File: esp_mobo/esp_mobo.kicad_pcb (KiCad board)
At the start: 2 copper layers, 75.5 x 107 mm, 54 parts, among them J1 Conn_01x04_Pin, J10 Conn_01x03_Pin, J11 Conn_01x03_Pin, J12 Conn_01x03_Pin, J13 Conn_01x03_Pin, J14 Conn_01x03_Pin, J15 Conn_01x03_Pin, J16 Conn_01x02_Pin, J2 Screw_Terminal_01x02, J3 Conn_01x03_Pin, J4 Conn_01x03_Pin, J5 Conn_01x03_Pin, J6 Conn_01x03_Pin, J7 Conn_01x03_Pin, J8 Conn_01x03_Pin, J9 Conn_01x03_Pin, U1 ESP32-DevKitC, U2 74AHCT125, U3 PC847, U4 PC847, U5 BME280

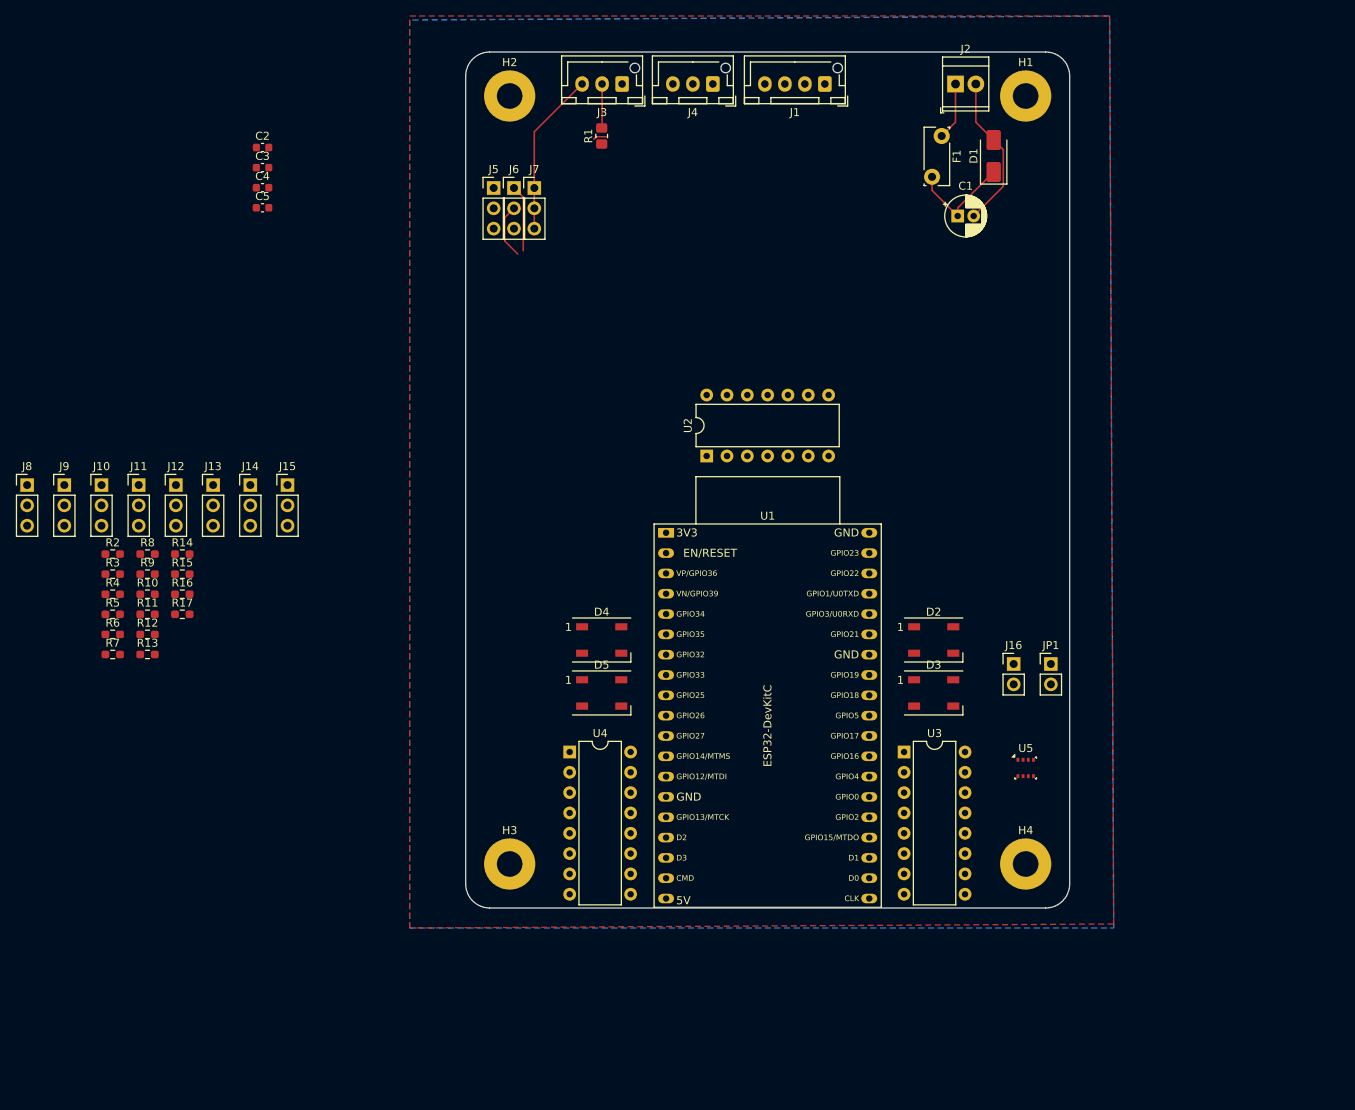
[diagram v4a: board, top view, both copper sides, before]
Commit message: Update ESC Mobo with board
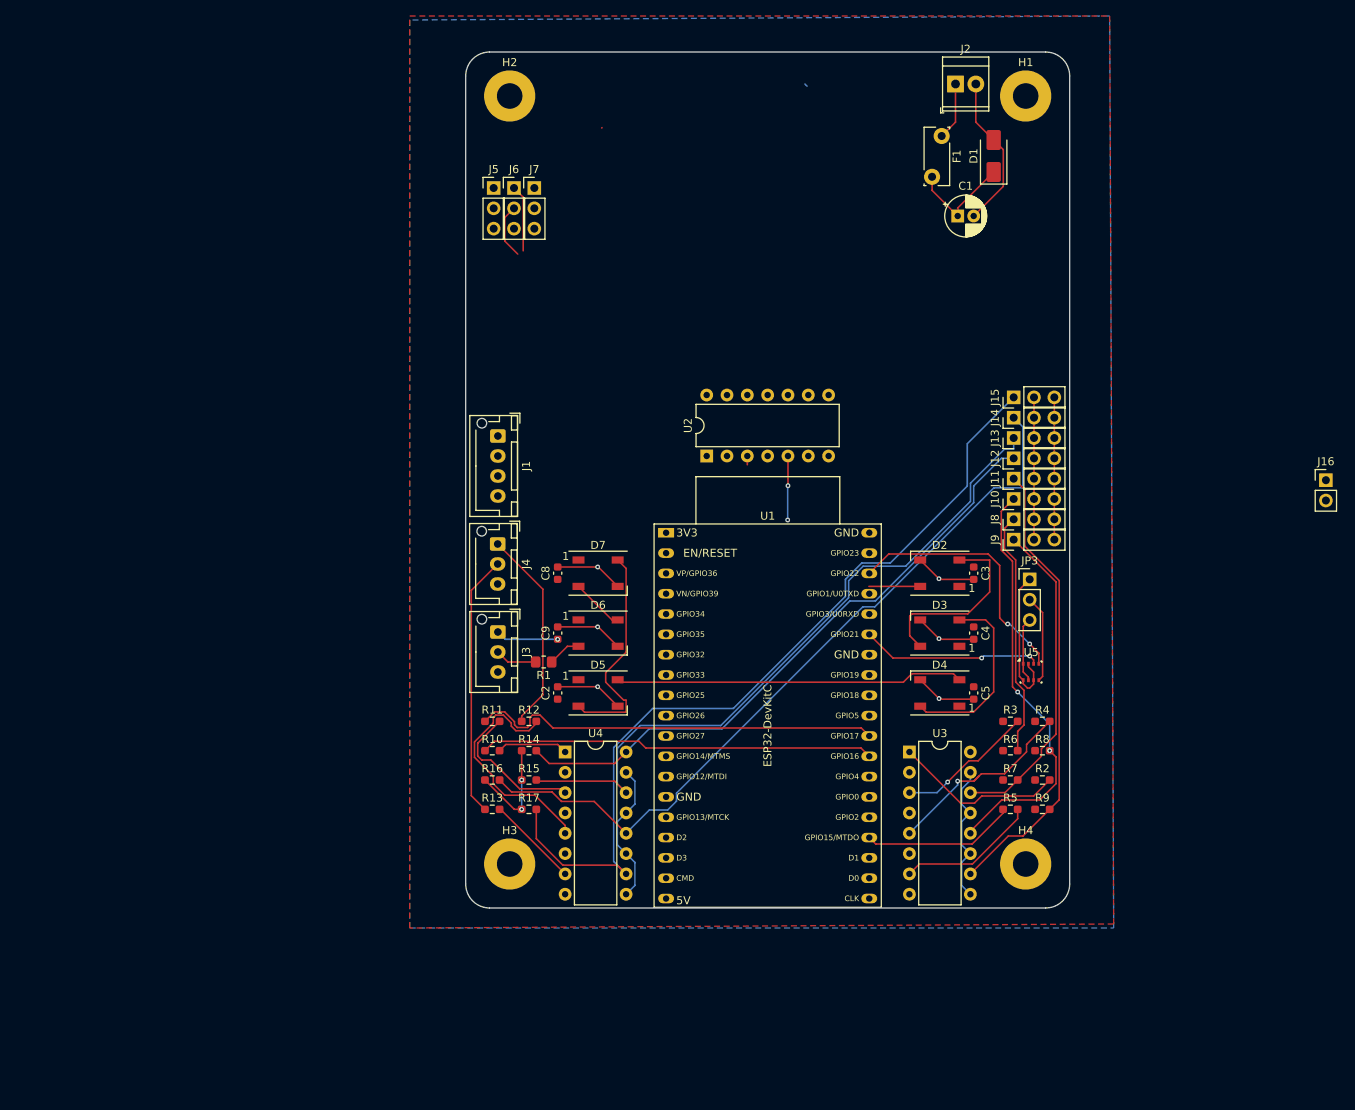
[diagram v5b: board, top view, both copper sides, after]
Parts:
- removed JP1: Jumper_2_Open, Connector_PinHeader_2.54mm:PinHeader_1x02_P2.54mm_Vertical
- added C8: 100uf, Capacitor_SMD:C_0603_1608Metric, F.Cu at (119.5, 99.7)
- added C9: 100uf, Capacitor_SMD:C_0603_1608Metric, F.Cu at (119.5, 107.1)
- added D6: WS2812B, LED_SMD:LED_WS2812B_PLCC4_5.0x5.0mm_P3.2mm, F.Cu at (124.5, 107.1)
- added D7: WS2812B, LED_SMD:LED_WS2812B_PLCC4_5.0x5.0mm_P3.2mm, F.Cu at (124.5, 99.7)
- added JP3: Jumper_3_Open, Connector_PinHeader_2.54mm:PinHeader_1x03_P2.54mm_Vertical, F.Cu at (178.5, 100.4)
- moved J8 123.4 mm to (176.5, 92.9), turned to 90 degrees
- moved R2 119.6 mm to (180.1, 125.5)
- moved J9 118.9 mm to (176.5, 95.5), turned to 90 degrees
- moved R4 117.3 mm to (180.1, 118.2)
- moved R9 115.7 mm to (180.1, 129.2)
- moved R5 114.8 mm to (176.1, 129.2)
- moved R8 114.5 mm to (180.1, 121.8)
- moved J10 114.0 mm to (176.5, 90.4), turned to 90 degrees
- moved R3 113.7 mm to (176.1, 118.2)
- moved R7 113.3 mm to (176.1, 125.5)
- moved R6 113.1 mm to (176.1, 121.8)
- moved J11 109.4 mm to (176.5, 87.8), turned to 90 degrees
- moved C5 107.6 mm to (171.5, 114.6), turned to 90 degrees
- moved C4 104.9 mm to (171.5, 107.1), turned to 90 degrees
- moved J12 104.8 mm to (176.5, 85.3), turned to 90 degrees
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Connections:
- D5 pad 2: Neopixel Data Out 5V -> Net-(D5-DOUT)
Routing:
- net Motor 8 Out: track 0.00 -> 105.6 mm
- net Motor 7 Out: track 0.00 -> 95.9 mm
- net Motor 6 Out: track 0.00 -> 86.9 mm
- net Motor 5 Out: track 0.00 -> 77.4 mm
- net Motor 4 Out: track 0.00 -> 57.4 mm
- net GNDPWR: track 0.00 -> 53.7 mm
- net Motor 3 Out: track 0.00 -> 52.5 mm, vias 0 -> 2
- net Motor 6 Signal: track 0.00 -> 51.8 mm
- net Motor 5 Signal: track 0.00 -> 49.3 mm
- net Net-(D4-DOUT): track 0.00 -> 43.6 mm
- net Motor 2 Out: track 0.00 -> 40.8 mm
- net GND: track 40.0 -> 76.2 mm, vias 0 -> 6
- net Motor 8 Signal: track 0.00 -> 32.7 mm
- net SCL: track 0.00 -> 32.5 mm, vias 0 -> 2
- net Vdrive: track 0.00 -> 31.2 mm, vias 0 -> 2
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
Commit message: Update ESC Mobo Silkscreen
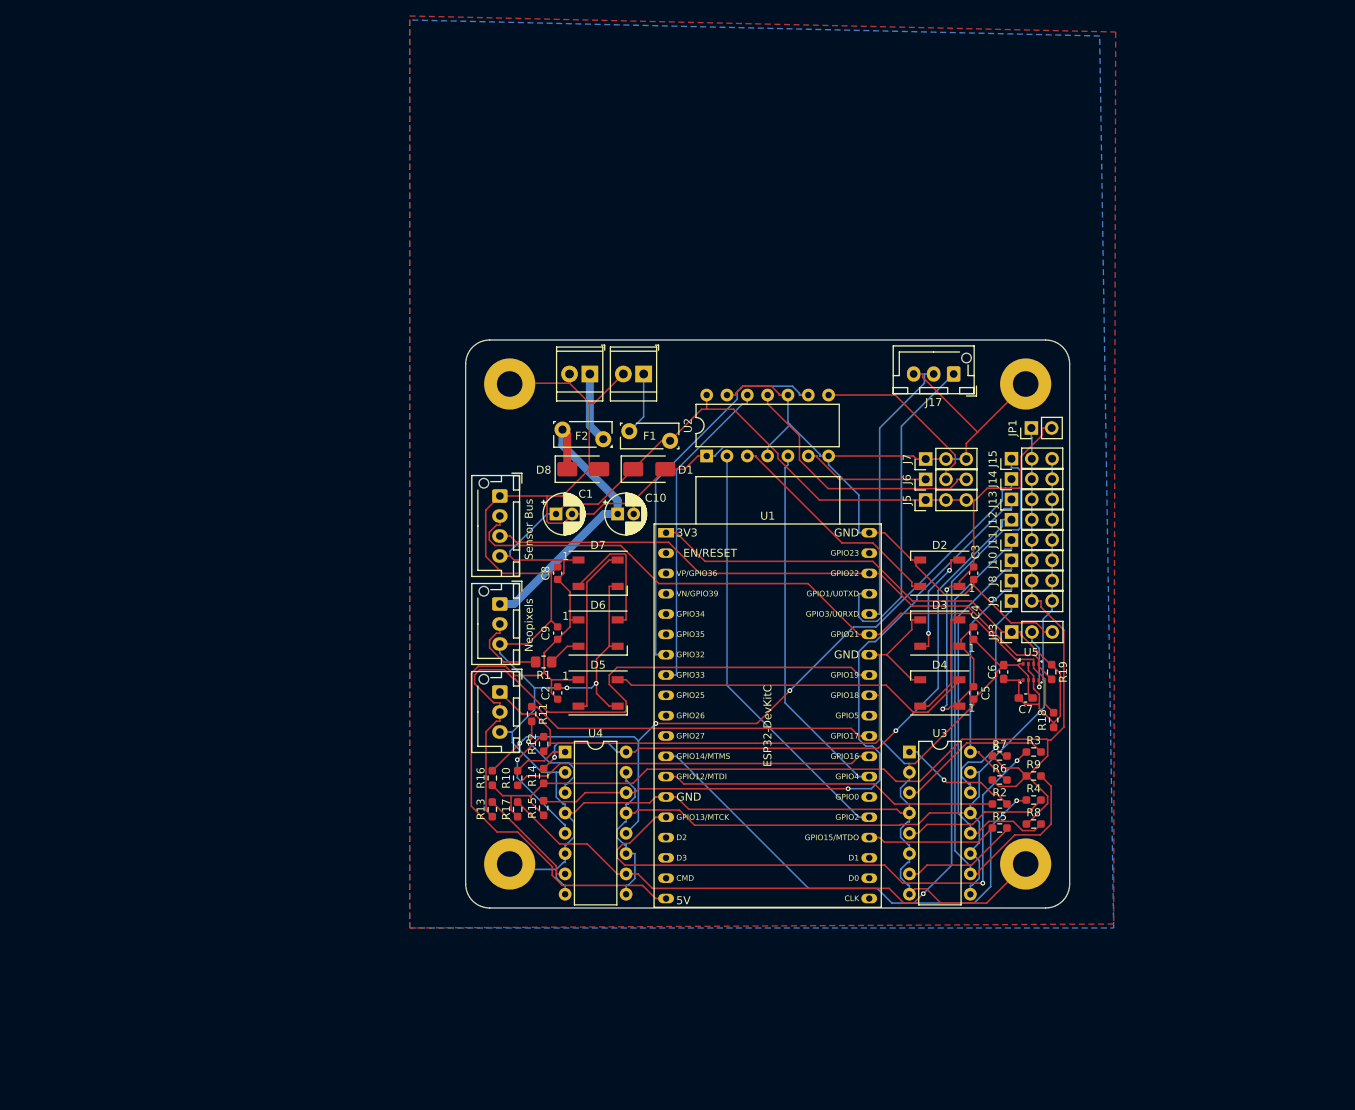
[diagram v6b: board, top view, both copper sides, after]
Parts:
- added C10: C_Polarized, Capacitor_THT:CP_Radial_D5.0mm_P2.00mm, F.Cu at (127.0, 92.2)
- added C6: 100nF, Capacitor_SMD:C_0603_1608Metric_Pad1.08x0.95mm_HandSolder, F.Cu at (175.2, 112.0)
- added C7: 100nF, Capacitor_SMD:C_0603_1608Metric_Pad1.08x0.95mm_HandSolder, F.Cu at (178.0, 115.2)
- added D8: SS14, Diode_SMD:D_SMA, F.Cu at (122.7, 86.7)
- added F2: Polyfuse, Fuse:Fuse_Bourns_MF-RG300, F.Cu at (125.2, 82.9)
- added J17: Conn_01x03_Pin, Connector_JST:JST_XH_B3B-XH-AM_1x03_P2.50mm_Vertical, F.Cu at (169.0, 74.8)
- added JP1: Jumper_2_Open, Connector_PinHeader_2.54mm:PinHeader_1x02_P2.54mm_Vertical, F.Cu at (178.7, 81.5)
- added R18: 4.7K, Resistor_SMD:R_0603_1608Metric_Pad0.98x0.95mm_HandSolder, F.Cu at (181.5, 118.0)
- added R19: 4.7K, Resistor_SMD:R_0603_1608Metric_Pad0.98x0.95mm_HandSolder, F.Cu at (181.2, 112.0)
- C2, C3, C4, C5, C8, C9: value 100uf -> 100nf
- J16: value Conn_01x02_Pin -> Screw_Terminal_01x02; footprint Connector_PinHeader_2.54mm:PinHeader_1x02_P2.54mm_Vertical -> TerminalBlock_TE-Connectivity:TerminalBlock_TE_282834-2_1x02_P2.54mm_Horizontal
- Sensor Bus1: renamed from J1
- moved J16 93.0 mm to (123.5, 74.8), turned to 180 degrees
- moved J5 66.6 mm to (165.5, 90.5), turned to 90 degrees
- moved J6 63.0 mm to (165.5, 87.9), turned to 90 degrees
- moved C1 62.5 mm to (119.3, 92.2)
- moved J7 59.5 mm to (165.5, 85.4), turned to 90 degrees
- moved D1 58.2 mm to (130.9, 86.7), turned to 0 degrees
- moved F1 53.7 mm to (128.4, 81.9), turned to 0 degrees
- moved J2 53.2 mm to (130.2, 74.8), turned to 180 degrees
- moved H1 36.0 mm to (178.0, 76.0)
- moved H2 36.0 mm to (113.5, 76.0)
- moved I2CMot1 18.5 mm to (112.3, 114.5)
- moved R4 9.89 mm to (179.0, 128.0)
- moved R8 9.23 mm to (179.0, 131.0)
- moved J10 7.67 mm to (176.2, 98.0)
- moved J11 7.67 mm to (176.2, 95.5)
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- renumbered J4 to I2CMot1
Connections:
- J16 pad 1: +5V -> Net-(J16-Pin_1)
- J16 pad 2: Vdrive -> GND
- J3 pad 1: +5V -> +12V
- Sensor Bus1 pad 1: +5V -> GND
- Sensor Bus1 pad 4: GND -> +5V
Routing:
- net GND: track 76.2 -> 440.1 mm, vias 6 -> 2
- net +5V: track 21.4 -> 224.4 mm, vias 1 -> 2
- net Vdrive: track 31.2 -> 147.0 mm, vias 2 -> 0
- net Motor 2 Signal: track 0.00 -> 74.5 mm, vias 0 -> 2
- net GNDPWR: track 53.7 -> 126.0 mm
- net SDA: track 23.3 -> 87.9 mm, vias 2 -> 0
- net Motor 3 Signal: track 0.00 -> 62.4 mm, vias 0 -> 1
- net +3.3V: track 18.3 -> 80.2 mm
- net Neopixel Data Out 3.3V: track 0.00 -> 53.3 mm
- net Motor 8 Signal: track 32.7 -> 80.9 mm
- net Servo2 Data In: track 0.00 -> 48.1 mm
- net SCL: track 32.5 -> 77.0 mm, vias 2 -> 0
- net Motor 1 Signal: track 0.00 -> 42.2 mm
- net TX: track 0.00 -> 41.6 mm
- net Servo3 Data In: track 0.00 -> 40.3 mm
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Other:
- board size 75.5 x 107 mm -> 75.5 x 71 mm
- board text added: "Neopixels"
- board text added: "Sensor Bus"

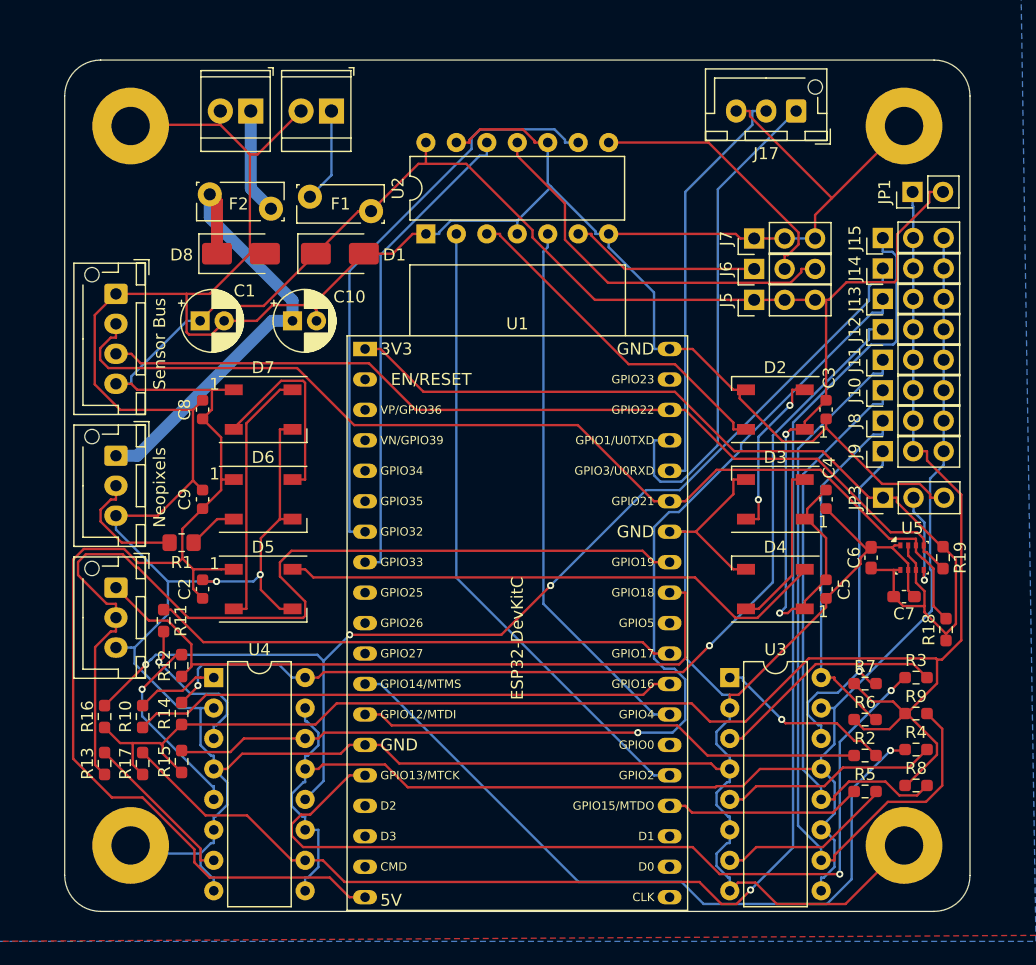
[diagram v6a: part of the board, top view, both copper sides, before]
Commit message: Update ESC Mobo Ground Points
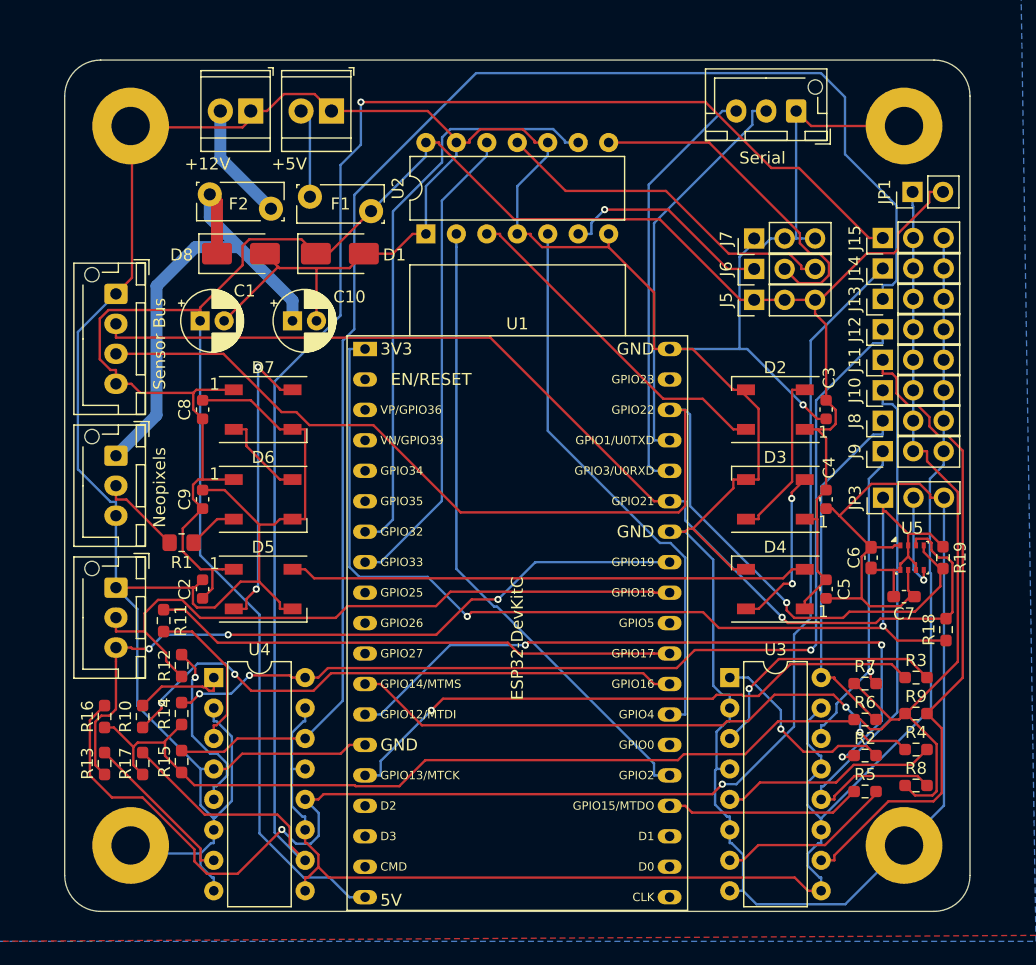
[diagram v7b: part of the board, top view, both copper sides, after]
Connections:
- F1 pad 1: Net-(J2-Pin_1) -> Net-(J2-Pin_2)
- F2 pad 1: Net-(J16-Pin_1) -> Net-(J16-Pin_2)
- I2CMot1 pad 1: Motor 7 Signal -> GND
- I2CMot1 pad 2: Motor 8 Signal -> Motor 7 Signal
- I2CMot1 pad 3: GND -> Motor 8 Signal
- J16 pad 1: Net-(J16-Pin_1) -> GND
- J16 pad 2: GND -> Net-(J16-Pin_2)
- J17 pad 1: TX -> GND
- J17 pad 2: RX -> TX
- J17 pad 3: GND -> RX
- J2 pad 1: Net-(J2-Pin_1) -> GND
- J2 pad 2: GND -> Net-(J2-Pin_2)
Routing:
- net Motor 6 Out: track 88.8 -> 123.3 mm, vias 1 -> 0
- net Motor 7 Out: track 94.0 -> 119.8 mm, vias 3 -> 2
- net SCL: track 77.0 -> 102.4 mm, vias 0 -> 1
- net Motor 2 Signal: track 74.5 -> 50.1 mm, vias 2 -> 1
- net Motor 8 Signal: track 80.9 -> 61.2 mm, vias 0 -> 3
- net +3.3V: track 80.2 -> 99.8 mm, vias 0 -> 2
- net GND: track 440.1 -> 456.2 mm, vias 2 -> 1
- net Motor 8 Out: track 117.9 -> 133.8 mm
- net Motor 1 Signal: track 42.2 -> 57.6 mm, vias 0 -> 3
- net Motor 3 Signal: track 62.4 -> 49.9 mm, vias 1 -> 2
- net Motor 4 Out: track 65.5 -> 54.6 mm
- net Net-(J16-Pin_2): track 0.00 -> 9.90 mm
- net Net-(D6-DIN): track 16.9 -> 7.45 mm
- net Net-(J16-Pin_1): track 8.85 -> 0.00 mm
- net TX: track 41.6 -> 33.3 mm
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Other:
- board text added: "+12V"
- board text added: "+5V"
- board text added: "Serial"

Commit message: Lots of changes
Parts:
- added R20: 20K, Resistor_SMD:R_0603_1608Metric_Pad0.98x0.95mm_HandSolder, F.Cu at (148.0, 101.0)
- added R21: 10K, Resistor_SMD:R_0603_1608Metric_Pad0.98x0.95mm_HandSolder, F.Cu at (117.2, 87.2)
- added R22: 10K, Resistor_SMD:R_0603_1608Metric_Pad0.98x0.95mm_HandSolder, F.Cu at (118.7, 96.2)
- added R23: 10K, Resistor_SMD:R_0603_1608Metric_Pad0.98x0.95mm_HandSolder, F.Cu at (113.8, 123.8)
- added R24: 10K, Resistor_SMD:R_0603_1608Metric_Pad0.98x0.95mm_HandSolder, F.Cu at (119.5, 118.2)
- added R25: 20K, Resistor_SMD:R_0603_1608Metric_Pad0.98x0.95mm_HandSolder, F.Cu at (147.8, 91.8)
- added U6: TMCS1100A2QDR, TMCS1100A2QDR:SOIC8_D_TEX, F.Cu at (143.2, 102.8)
- added U7: LM4030-2.5, Package_TO_SOT_SMD:SOT-23-5, F.Cu at (149.2, 104.5)
- added U8: TMCS1100A2QDR, TMCS1100A2QDR:SOIC8_D_TEX, F.Cu at (143.0, 93.2)
- added U9: LM4030-2.5, Package_TO_SOT_SMD:SOT-23-5, F.Cu at (149.0, 95.2)
- moved R18 38.0 mm to (144.5, 109.5), turned to 0 degrees
- moved R19 35.7 mm to (145.6, 111.2), turned to 0 degrees
- moved C7 34.1 mm to (143.9, 116.6)
- moved U5 33.6 mm to (145.2, 113.8)
- moved C6 32.8 mm to (142.5, 113.8)
- moved R10 1.27 mm to (114.8, 126.5)
- moved R13 1.27 mm to (111.6, 130.4)
- moved R16 1.27 mm to (111.6, 126.5)
- moved R17 1.27 mm to (114.8, 130.4)
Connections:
- C1 pad 1: +5V -> 5VInput
- C10 pad 1: +12V -> NeoPowerIn
- D1 pad 1: +5V -> 5VInput
- D8 pad 1: +12V -> NeoPowerIn
- F1 pad 2: +5V -> 5VInput
- F2 pad 2: +12V -> NeoPowerIn
- J3 pad 1: +12V -> NeoPowerOut
- U1 pad 5: unconnected-(U1-VDET_1/GPIO34/ADC1_CH6-Pad5) -> CurrentSensNeoPix
- U1 pad 6: unconnected-(U1-VDET_2/GPIO35/ADC1_CH7-Pad6) -> CurrentSens5V
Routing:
- net +3.3V: track 99.8 -> 153.4 mm, vias 2 -> 4
- net NeoPowerOut: track 0.00 -> 44.6 mm, vias 0 -> 1
- net +12V: track 42.4 -> 0.00 mm
- net NeoPowerIn: track 0.00 -> 42.3 mm
- net SCL: track 102.4 -> 60.6 mm, vias 1 -> 0
- net Motor 6 Out: track 123.3 -> 84.1 mm, vias 0 -> 1
- net 5VInput: track 0.00 -> 36.2 mm
- net Net-(JP3-C): track 8.07 -> 39.6 mm, vias 1 -> 0
- net SDA: track 91.0 -> 120.5 mm, vias 1 -> 0
- net Motor 8 Out: track 133.8 -> 105.0 mm
- net Motor 8 Signal: track 61.2 -> 89.9 mm, vias 3 -> 1
- net Motor 2 Signal: track 50.1 -> 73.3 mm, vias 1 -> 3
- net CurrentSens5V: track 0.00 -> 22.2 mm, vias 0 -> 1
- net GND: track 456.2 -> 473.4 mm
- net Motor 4 Out: track 54.6 -> 71.5 mm
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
